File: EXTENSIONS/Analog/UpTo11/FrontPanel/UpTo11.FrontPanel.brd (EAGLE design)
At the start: 48 x 38 mm, 9 parts, among them X1 USB-A

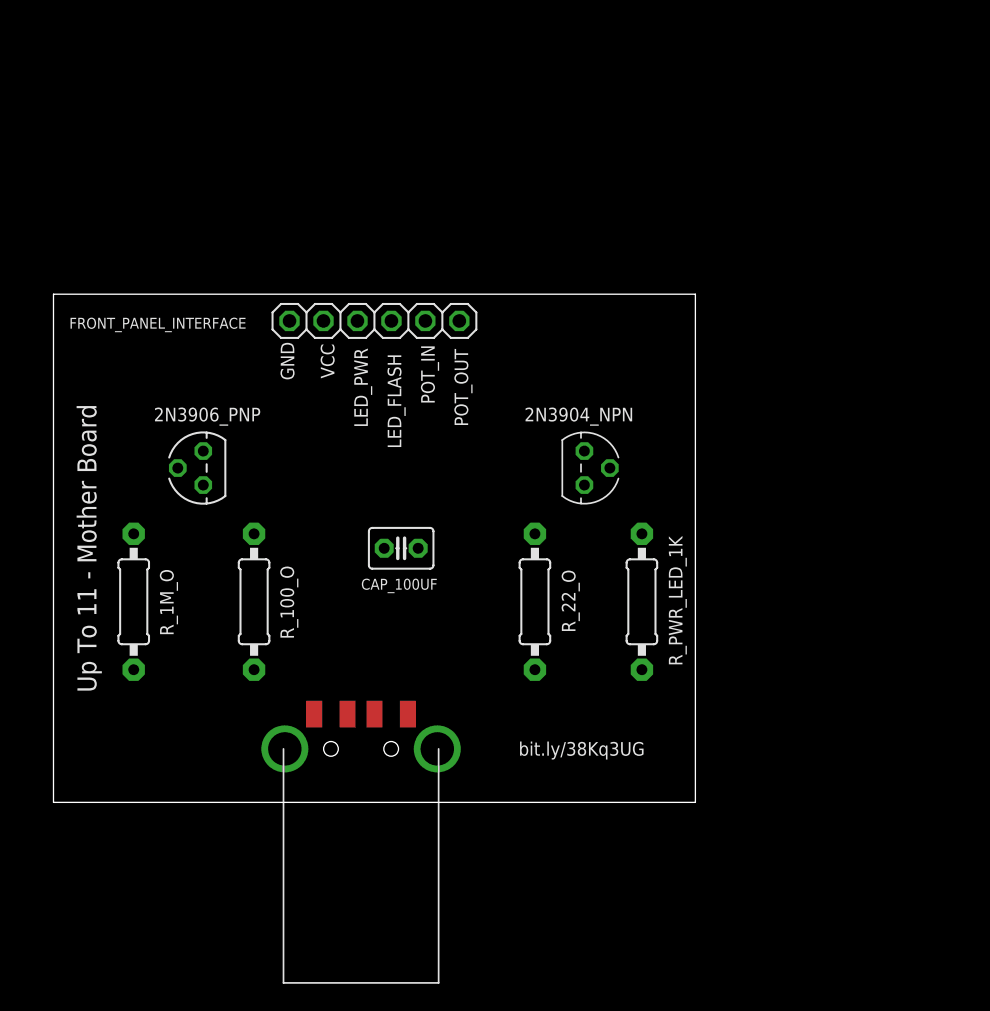
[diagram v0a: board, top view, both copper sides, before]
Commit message: Create UpTo11 Front Panel
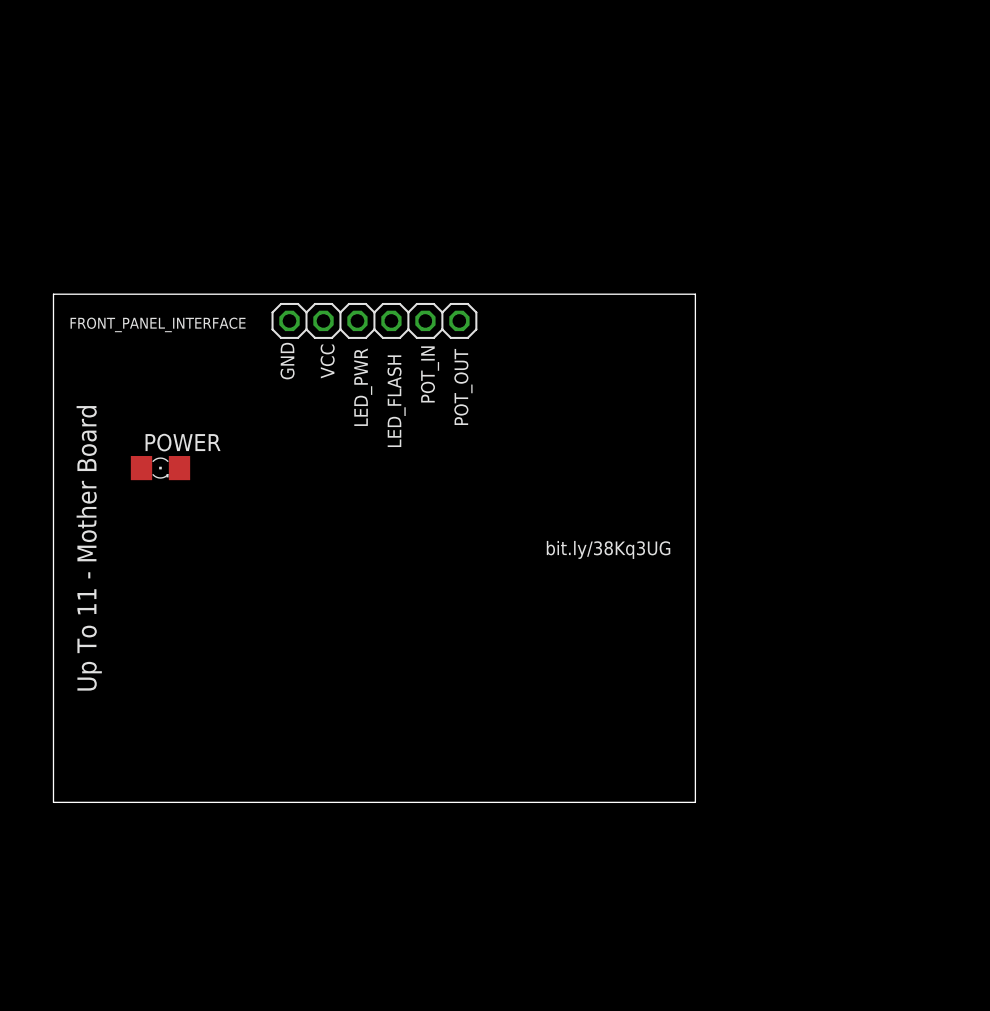
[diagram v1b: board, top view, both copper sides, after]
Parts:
- removed 2N3904_NPN: 2N3904, transistor:TO92
- removed 2N3906_PNP: 2N3906, transistor-pnp:TO92
- removed CAP_100UF: (no value), adafruit:C025-030X050
- removed R_100_O, R_1M_O, R_22_O, R_PWR_LED_1K: (no value), adafruit:0207/10
- removed X1: USB-A, adafruit:MOLEX_480371000
- added POWER: (no value), adafruit:1206
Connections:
- removed net N$2: 2N3904_NPN.1, CAP_100UF.2, R_22_O.1
- removed net N$5: 2N3906_PNP.2, CAP_100UF.1, R_1M_O.2
- removed net N$6: 2N3906_PNP.1, R_100_O.1
- net GND_EX: now also POWER.C; no longer R_1M_O.1, X1.4
- net LED_FLASH: no longer 2N3904_NPN.3
- net LED_PWR: now also POWER.A; no longer R_PWR_LED_1K.1
- net POT_IN: no longer R_100_O.2
- net POT_OUT: no longer 2N3904_NPN.2
- net VCC: no longer 2N3906_PNP.3, R_22_O.2, R_PWR_LED_1K.2, X1.1
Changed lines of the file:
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@@
 <text x="48.5" y="27" size="1.4224" layer="26" rot="MR270" align="center">www.FredericTorres.com</text>
 <text x="25" y="42" size="1.6764" layer="26" rot="MR0" align="center">https://bit.ly/38Kq3UG</text>
-<text x="41.5" y="16" size="1.016" layer="25" align="center">bit.ly/38Kq3UG</text>
+<text x="43.5" y="31" size="1.016" layer="25" align="center">bit.ly/38Kq3UG</text>
 <text x="19.5" y="45" size="1.016" layer="25" rot="R90" align="center">GND</text>
 <text x="22.5" y="45" size="1.016" layer="25" rot="R90" align="center">VCC</text>
@@
 </autorouter>
 <elements>
-<element name="CAP_100UF" library="adafruit" package="C025-030X050" value="" x="28" y="31" smashed="yes">
-<attribute name="NAME" x="25" y="27.905" size="0.8128" layer="25" ratio="10"/>
-<attribute name="VALUE" x="25.714" y="27.952" size="1.27" layer="27" ratio="10"/>
-</element>
-<element name="R_100_O" library="adafruit" package="0207/10" value="" x="17" y="27" smashed="yes" rot="R90">
-<attribute name="NAME" x="19.476" y="26.952" size="1.016" layer="25" ratio="10" rot="R90" align="center"/>
-<attribute name="VALUE" x="17.635" y="24.7394" size="1.27" layer="27" ratio="10" rot="R90"/>
-</element>
-<element name="R_22_O" library="adafruit" package="0207/10" value="" x="38" y="27" smashed="yes" rot="R270">
-<attribute name="NAME" x="40.524" y="27.048" size="1.016" layer="25" ratio="10" rot="R270" align="center"/>
-<attribute name="VALUE" x="37.365" y="29.2606" size="1.27" layer="27" ratio="10" rot="R270"/>
-</element>
-<element name="R_1M_O" library="adafruit" package="0207/10" value="" x="8" y="27" smashed="yes" rot="R90">
-<attribute name="NAME" x="10.476" y="26.952" size="1.016" layer="25" ratio="10" rot="R90" align="center"/>
-<attribute name="VALUE" x="8.635" y="24.7394" size="1.27" layer="27" ratio="10" rot="R90"/>
-</element>
-<element name="2N3904_NPN" library="transistor" package="TO92" value="2N3904" x="41.7" y="37" smashed="yes" rot="R270">
-<attribute name="NAME" x="41.3" y="41" size="1.016" layer="25" ratio="10" align="center"/>
-</element>
-<element name="2N3906_PNP" library="transistor-pnp" package="TO92" value="2N3906" x="13.2" y="37" smashed="yes" rot="R90">
-<attribute name="NAME" x="13.5" y="41" size="1.016" layer="25" ratio="10" align="center"/>
-</element>
-<element name="X1" library="adafruit" package="MOLEX_480371000" value="USB-A" x="25" y="16" smashed="yes">
-<attribute name="VALUE" x="23.46" y="12.65" size="1.016" layer="27" font="vector"/>
-</element>
 <element name="FRONT_PANEL_INTERFACE" library="adafruit" package="1X06" value="" x="26" y="48" smashed="yes">
 <attribute name="NAME" x="9.8038" y="47.8288" size="0.8128" layer="25" ratio="10" align="center"/>
 <attribute name="VALUE" x="18.38" y="44.825" size="1.27" layer="27"/>
 </element>
-<element name="R_PWR_LED_1K" library="adafruit" package="0207/10" value="" x="46" y="27" smashed="yes" rot="R270">
-<attribute name="NAME" x="48.524" y="27.048" size="1.016" layer="25" ratio="10" rot="R270" align="center"/>
-<attribute name="VALUE" x="45.365" y="29.2606" size="1.27" layer="27" ratio="10" rot="R270"/>
-</element>
+<element name="POWER" library="adafruit" package="1206" value="" x="10" y="37"/>
 </elements>
 <signals>
-<signal name="N$2">
-<contactref element="R_22_O" pad="1"/>
-<contactref element="2N3904_NPN" pad="1"/>
-<contactref element="CAP_100UF" pad="2"/>
-<wire x1="38" y1="32.08" x2="41.7" y2="35.73" width="0" layer="19" extent="1-1"/>
-<wire x1="29.27" y1="31" x2="38" y2="32.08" width="0" layer="19" extent="1-1"/>
-</signal>
 <signal name="LED_FLASH">
-<contactref element="2N3904_NPN" pad="3"/>
 <contactref element="FRONT_PANEL_INTERFACE" pad="4"/>
-<wire x1="27.27" y1="48" x2="41.7" y2="38.27" width="0" layer="19" extent="1-1"/>
 </signal>
 <signal name="GND_EX">
-<contactref element="X1" pad="4"/>
-<contactref element="R_1M_O" pad="1"/>
 <contactref element="FRONT_PANEL_INTERFACE" pad="1"/>
-<wire x1="8" y1="21.92" x2="19.65" y2="48" width="0" layer="19" extent="1-1"/>
-<wire x1="21.5" y1="18.6" x2="8" y2="21.92" width="0" layer="19" extent="1-1"/>
-</signal>
-<signal name="N$5">
-<contactref element="CAP_100UF" pad="1"/>
-<contactref element="2N3906_PNP" pad="2"/>
-<contactref element="R_1M_O" pad="2"/>
-<wire x1="11.295" y1="37" x2="26.73" y2="31" width="0" layer="19" extent="1-1"/>
-<wire x1="8" y1="32.08" x2="11.295" y2="37" width="0" layer="19" extent="1-1"/>
-</signal>
-<signal name="N$6">
-<contactref element="2N3906_PNP" pad="1"/>
-<contactref element="R_100_O" pad="1"/>
-<wire x1="17" y1="21.92" x2="13.2" y2="38.27" width="0" layer="19" extent="1-1"/>
+<contactref element="POWER" pad="C"/>
+<wire x1="11.422" y1="37" x2="19.65" y2="48" width="0" layer="19" extent="1-1"/>
 </signal>
 <signal name="VCC">
 <contactref element="FRONT_PANEL_INTERFACE" pad="2"/>
-<contactref element="X1" pad="1"/>
-<contactref element="R_22_O" pad="2"/>
-<contactref element="2N3906_PNP" pad="3"/>
-<contactref element="R_PWR_LED_1K" pad="2"/>
-<wire x1="13.2" y1="35.73" x2="22.19" y2="48" width="0" layer="19" extent="1-1"/>
-<wire x1="28.5" y1="18.6" x2="13.2" y2="35.73" width="0" layer="19" extent="1-1"/>
-<wire x1="38" y1="21.92" x2="28.5" y2="18.6" width="0" layer="19" extent="1-1"/>
-<wire x1="46" y1="21.92" x2="38" y2="21.92" width="0" layer="19" extent="1-1"/>
 </signal>
 <signal name="LED_PWR">
-<contactref element="R_PWR_LED_1K" pad="1"/>
 <contactref element="FRONT_PANEL_INTERFACE" pad="3"/>
-<wire x1="24.73" y1="48" x2="46" y2="32.08" width="0" layer="19" extent="1-1"/>
+<contactref element="POWER" pad="A"/>
+<wire x1="8.578" y1="37" x2="24.73" y2="48" width="0" layer="19" extent="1-1"/>
 </signal>
 <signal name="POT_IN">
-<contactref element="R_100_O" pad="2"/>
 <contactref element="FRONT_PANEL_INTERFACE" pad="5"/>
-<wire x1="17" y1="32.08" x2="29.81" y2="48" width="0" layer="19" extent="1-1"/>
 </signal>
 <signal name="POT_OUT">
-<contactref element="2N3904_NPN" pad="2"/>
 <contactref element="FRONT_PANEL_INTERFACE" pad="6"/>
-<wire x1="32.35" y1="48" x2="43.605" y2="37" width="0" layer="19" extent="1-1"/>
 </signal>
 </signals>

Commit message: Create UpTo11 Front Panel
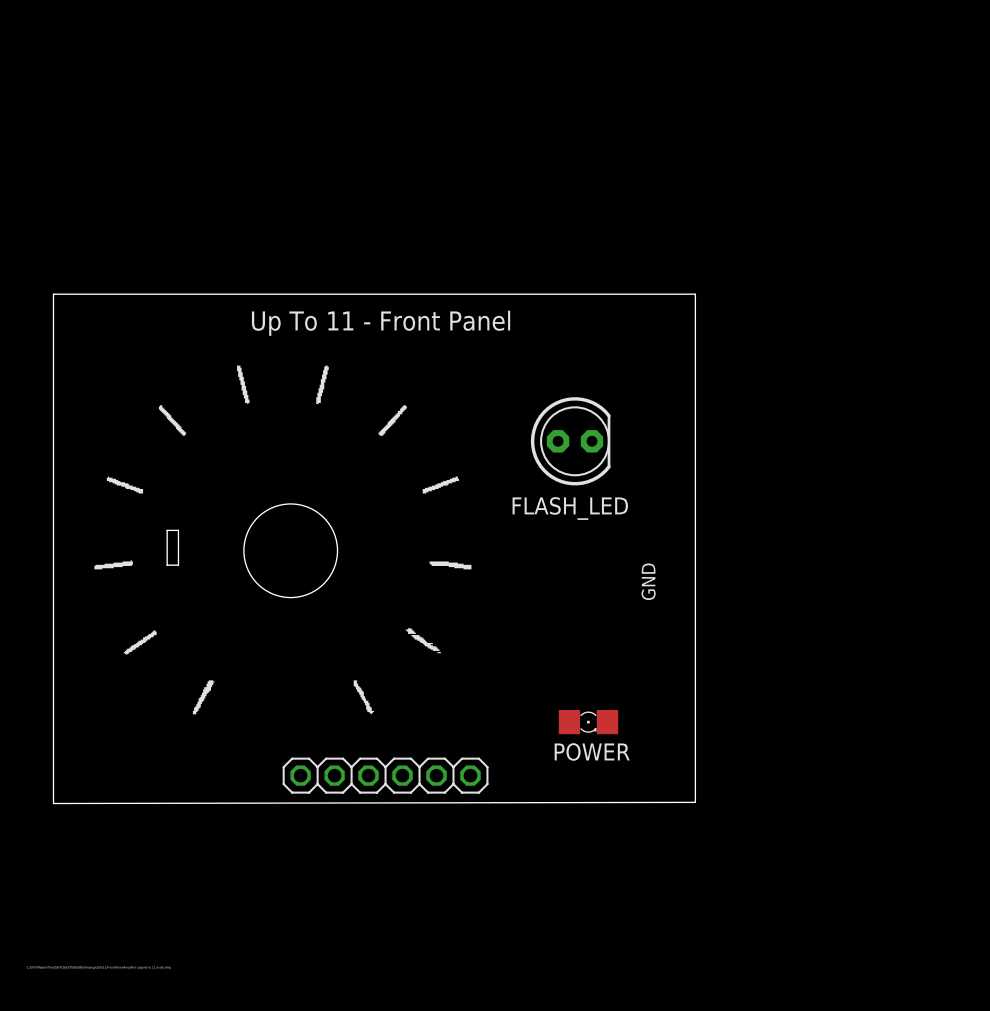
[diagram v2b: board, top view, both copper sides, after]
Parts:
- added FLASH_LED: (no value), adafruit:LED5MM
- moved POWER 37.2 mm to (42.0, 18.0)
- moved FRONT_PANEL_INTERFACE 34.0 mm to (26.8, 14.0)
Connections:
- net GND_EX: now also FLASH_LED.K
- net LED_FLASH: now also FLASH_LED.A
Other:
- board size 48 x 38 mm -> 48 x 38.1 mm
- board text added: "C:/DVT/MadeInTheUSB.PCB/EXTENSIONS/Analog/UpTo11/FrontPanel/Amplifier Legend to 11.mask.bmp"
- board text added: "Up To 11 - Front Panel"
- board text added: "https://bit.ly/2Pm6jPo"
- board text removed: "LED_FLASH"
- board text removed: "LED_PWR"
- board text removed: "POT_IN"
- board text removed: "POT_OUT"
- board text removed: "Up To 11 - Mother Board"
- board text removed: "Up To 11 - MotherBoard"
- board text removed: "VCC"
- board text removed: "bit.ly/38Kq3UG"
- board text removed: "https://bit.ly/38Kq3UG"

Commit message: Create UpTo11 Front Panel
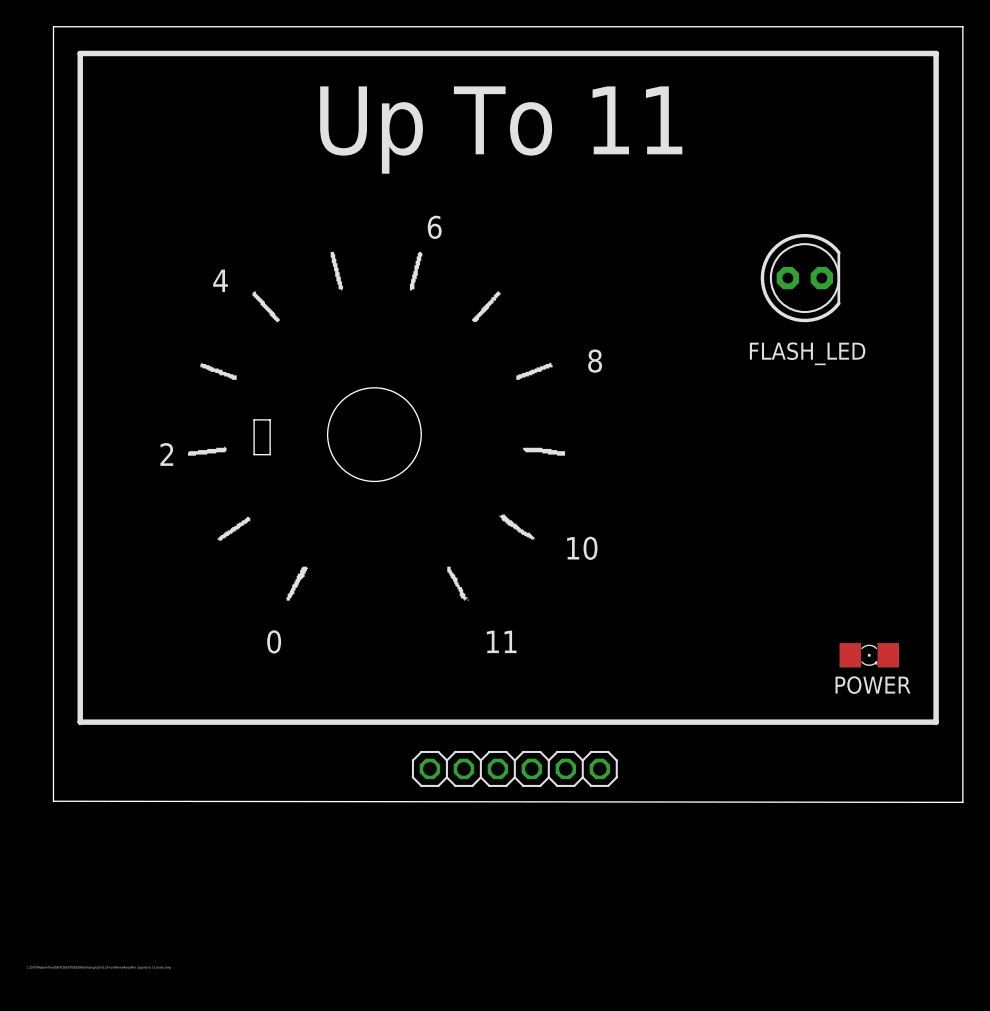
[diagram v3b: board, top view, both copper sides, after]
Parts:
- moved POWER 21.6 mm to (63.0, 23.0)
- moved FLASH_LED 21.1 mm to (58.2, 51.2)
- moved FRONT_PANEL_INTERFACE 9.68 mm to (36.5, 14.5), turned to 180 degrees
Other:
- board size 48 x 38.1 mm -> 68 x 58 mm
- board text added: "0"
- board text added: "10"
- board text added: "11"
- board text added: "2"
- board text added: "4"
- board text added: "6"
- board text added: "8"
- board text added: "LED_FLASH"
- board text added: "LED_PWR"
- board text added: "POT_IN"
- board text added: "POT_OUT"
- board text added: "Up To 11"
- board text added: "Up To 11 - MotherBoard"
- board text added: "VCC"
- board text added: "https://bit.ly/38Kq3UG"
- board text removed: "Up To 11 - Front Panel"
- board text removed: "https://bit.ly/2Pm6jPo"
